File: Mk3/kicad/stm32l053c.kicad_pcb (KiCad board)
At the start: 2 copper layers, 27.2 x 21.8 mm, 29 parts, among them J1 LIGHT+, J2 LIGHT-, P1 SWD, U1 AP2112, U2 STM32L053C8_LQFP48, U3 ADS1015, U4 UFL_SMA, U5 RFM92/95

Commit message: Start of traces
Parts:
- moved C1 4.89 mm to (141.2, 88.9), turned to 90 degrees
- moved C2 2.03 mm to (151.9, 91.2), turned to 270 degrees
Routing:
- net SWO: track 0.00 -> 21.8 mm, vias 0 -> 1
- net SWCLK: track 0.00 -> 20.5 mm, vias 0 -> 1
- net RFM_RST: track 0.00 -> 19.9 mm, vias 0 -> 1
- net SWDIO: track 0.00 -> 19.0 mm, vias 0 -> 1
- net DIO0: track 0.00 -> 14.8 mm, vias 0 -> 1
- net SPI1_MISO: track 0.00 -> 9.81 mm, vias 0 -> 1
- net SPI1_CS: track 0.00 -> 8.83 mm, vias 0 -> 1
- net /AIN2: track 0.00 -> 6.80 mm
- net SPI1_MOSI: track 0.00 -> 5.48 mm, vias 0 -> 1
- net SPI1_SCK: track 0.00 -> 4.49 mm, vias 0 -> 1
- net I2C1_SCL: track 0.00 -> 2.96 mm
- net I2C1_SDA: track 0.00 -> 2.89 mm

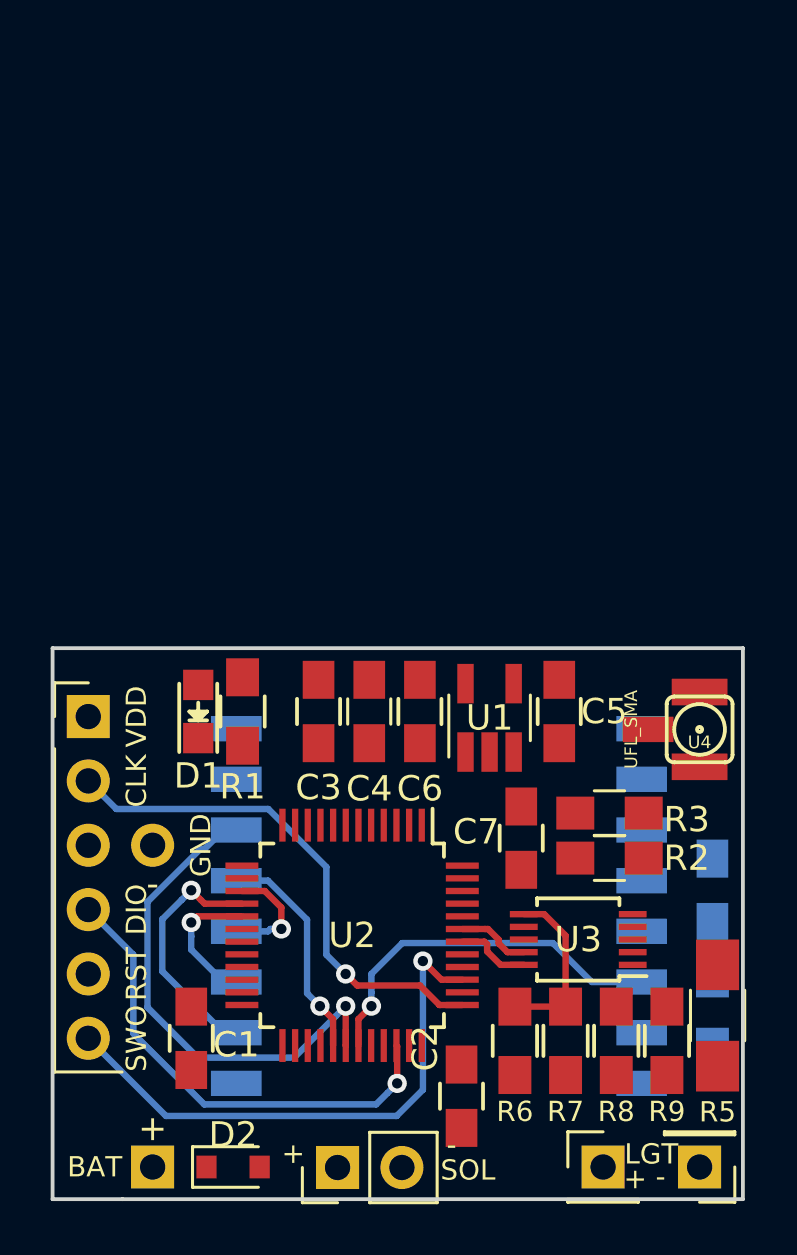
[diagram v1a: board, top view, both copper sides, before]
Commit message: Bigger board
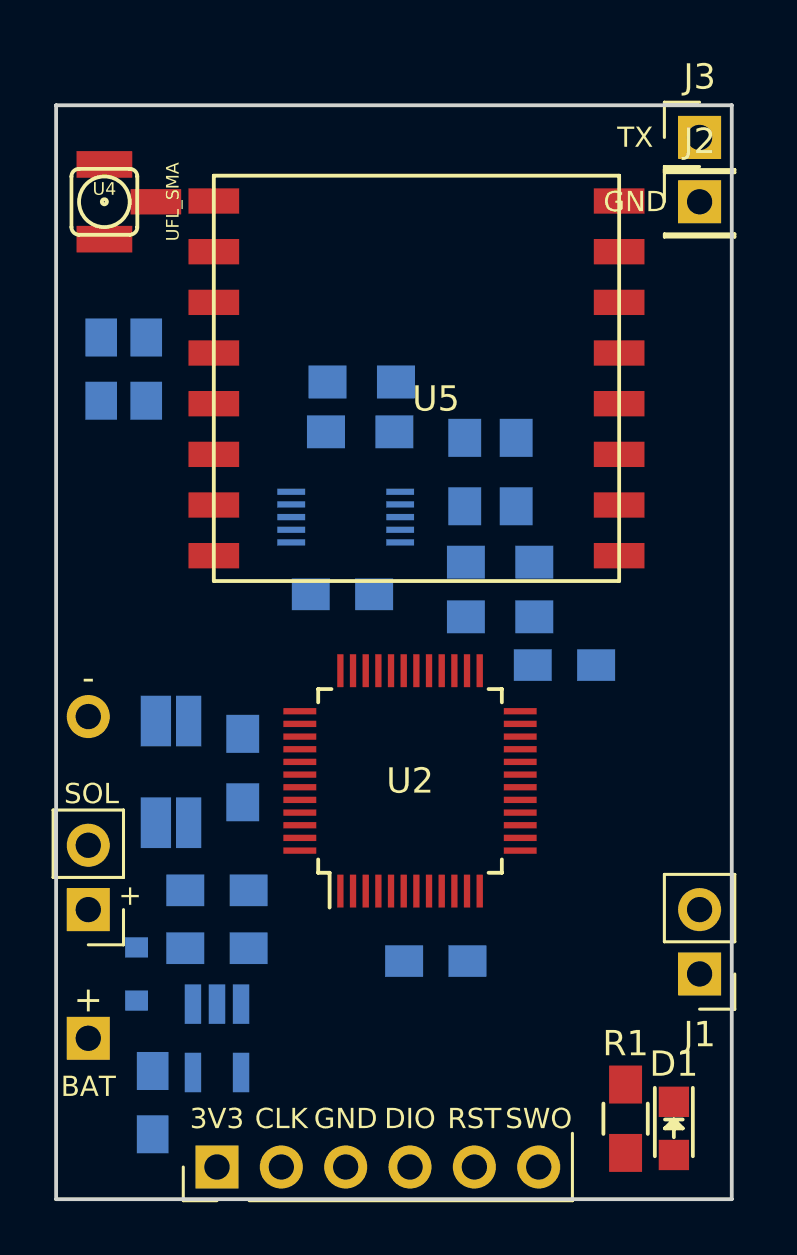
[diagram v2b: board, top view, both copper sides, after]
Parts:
- added J3: TX, Pin_Headers:Pin_Header_Straight_1x01_Pitch2.54mm, F.Cu at (161.3, 53.3)
- C1, C2, C3, C4, C5, C6, C7, D2, R2, R3, R6, R7, R8, R9, U1, U3: moved to B.Cu
- J1: value LIGHT+ -> LGT; footprint Pin_Headers:Pin_Header_Straight_1x01_Pitch2.54mm -> Pin_Headers:Pin_Header_Straight_1x02_Pitch2.54mm
- J2: value LIGHT- -> GND
- R5: value R -> R_Shunt; footprint Resistors_SMD:R_1206_HandSoldering -> theapi:SHUNT_1210_HandSoldering; moved to B.Cu
- U5: moved to F.Cu
- moved J2 38.1 mm to (161.3, 55.9), turned to 0 degrees
- moved U4 31.4 mm to (137.8, 55.9), turned to 90 degrees
- moved C8 30.4 mm to (139.4, 62.5)
- moved R8 27.9 mm to (148.0, 63.0), turned to 180 degrees
- moved R9 26.9 mm to (147.9, 65.0), turned to 180 degrees
- moved U5 25.7 mm to (158.1, 69.8), turned to 180 degrees
- moved D1 25.0 mm to (160.3, 92.5), turned to 270 degrees
- moved R5 23.6 mm to (140.5, 78.4)
- moved R6 22.5 mm to (152.0, 66.5), turned to 270 degrees
- moved R7 22.5 mm to (154.1, 66.5), turned to 90 degrees
- moved R1 22.1 mm to (158.4, 92.1), turned to 270 degrees
- moved R4 20.9 mm to (143.3, 78.2), turned to 90 degrees
- moved C1 20.8 mm to (156.0, 74.2), turned to 0 degrees
- moved U3 19.0 mm to (147.3, 68.3), turned to 0 degrees
- moved C6 18.7 mm to (139.7, 91.4)
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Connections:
- net /PA0 renamed LED
- net Net-(R8-Pad1) renamed /AIN3
- J2 pad 1: LIGHT- -> Earth
- P1 pad 6: SWO -> Net-(P1-Pad6)
- R5 pad 1: /AIN0_1 -> SOL_GND
- R5 pad 2: Earth -> /AIN0
- SC1 pad 2: /AIN0_1 -> SOL_GND
- U2 pad 11: ADC_RDY -> LGT_GND
- U2 pad 12: LIGHT- -> Net-(U2-Pad12)
- U2 pad 15: SPI1_SCK -> Net-(U2-Pad15)
- U2 pad 16: SPI1_MISO -> Net-(U2-Pad16)
- U2 pad 17: SPI1_MOSI -> Net-(U2-Pad17)
- U2 pad 21: Net-(U2-Pad21) -> DIO0
- U2 pad 22: Net-(U2-Pad22) -> RFM_RST
- U2 pad 25: Net-(U2-Pad25) -> SPI2_NSS
- U2 pad 26: Net-(U2-Pad26) -> SPI2_SCK
- U2 pad 27: Net-(U2-Pad27) -> SPI2_MISO
- U2 pad 28: Net-(U2-Pad28) -> SPI2_MOSI
- U2 pad 29: SPI1_CS -> Net-(U2-Pad29)
- U2 pad 30: RFM_RST -> USART1_TX
- U2 pad 31: DIO0 -> Net-(U2-Pad31)
- U2 pad 39: SWO -> Net-(U2-Pad39)
- U2 pad 41: Net-(U2-Pad41) -> ADC_RDY
- U3 pad 4: /AIN0_1 -> /AIN0
- U3 pad 5: Earth -> /AIN1
- U5 pad 2: SPI1_MISO -> SPI2_MISO
- U5 pad 3: SPI1_MOSI -> SPI2_MOSI
- U5 pad 4: SPI1_SCK -> SPI2_SCK
- U5 pad 5: SPI1_CS -> SPI2_NSS
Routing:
- net SWO: track 21.8 -> 0.00 mm, vias 1 -> 0
- net SWCLK: track 20.5 -> 0.00 mm, vias 1 -> 0
- net RFM_RST: track 19.9 -> 0.00 mm, vias 1 -> 0
- net SWDIO: track 19.0 -> 0.00 mm, vias 1 -> 0
- net DIO0: track 14.8 -> 0.00 mm, vias 1 -> 0
- net SPI1_MISO: track 9.81 -> 0.00 mm, vias 1 -> 0
- net SPI1_CS: track 8.83 -> 0.00 mm, vias 1 -> 0
- net /AIN2: track 6.80 -> 0.00 mm
- net SPI1_MOSI: track 5.48 -> 0.00 mm, vias 1 -> 0
- net SPI1_SCK: track 4.49 -> 0.00 mm, vias 1 -> 0
- net I2C1_SCL: track 2.96 -> 0.00 mm
- net I2C1_SDA: track 2.89 -> 0.00 mm
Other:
- board size 27.2 x 21.8 mm -> 26.7 x 43.2 mm
- board text added: "3V3"
- board text added: "TX"
- board text removed: "-"
- board text removed: "LGT"
- board text removed: "VDD"

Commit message: Routing
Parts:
- C2, C3, C4, C7, C8, R4: moved to F.Cu
- D2: footprint Diodes_SMD:D_0805 -> Diodes_SMD:D_1206
- moved R7 7.50 mm to (147.3, 63.2), turned to 180 degrees
- moved R8 5.46 mm to (152.9, 65.3), turned to 0 degrees
- moved R9 5.30 mm to (152.9, 63.2), turned to 0 degrees
- moved R6 4.87 mm to (147.3, 65.3), turned to 0 degrees
- moved C7 4.31 mm to (144.1, 74.4)
- moved C3 1.64 mm to (151.0, 87.5), turned to 270 degrees
- moved C2 1.52 mm to (143.8, 83.1)
- moved R4 0.54 mm to (143.6, 77.9)
- moved R5 0.52 mm to (140.0, 78.5)
- moved C5 0.51 mm to (142.7, 85.3)
- moved D2 0.25 mm to (139.3, 86.4)
- moved R1 0.18 mm to (158.2, 91.9)
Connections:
- U2 pad 21: DIO0 -> Net-(U2-Pad21)
- U2 pad 33: Net-(U2-Pad33) -> DIO0
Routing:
- net +3V3: track 0.00 -> 97.5 mm, vias 0 -> 2
- net USART1_TX: track 0.00 -> 27.3 mm
- net Net-(D2-Pad2): track 0.00 -> 26.0 mm, vias 0 -> 1
- net Net-(J1-Pad1): track 0.00 -> 24.6 mm
- net RFM_RST: track 0.00 -> 23.1 mm
- net SPI2_NSS: track 0.00 -> 20.8 mm
- net SWCLK: track 0.00 -> 20.4 mm, vias 0 -> 1
- net SWDIO: track 0.00 -> 20.3 mm, vias 0 -> 1
- net SPI2_SCK: track 0.00 -> 18.8 mm
- net I2C1_SDA: track 0.00 -> 17.4 mm, vias 0 -> 1
- net NRST: track 0.00 -> 16.0 mm, vias 0 -> 1
- net /AIN0: track 0.00 -> 15.8 mm
- net I2C1_SCL: track 0.00 -> 14.1 mm, vias 0 -> 1
- net LED: track 0.00 -> 13.0 mm
- net SPI2_MOSI: track 0.00 -> 12.2 mm
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
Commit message: Fully routed
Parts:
- C1: moved to F.Cu
- C7: moved to B.Cu
- moved C7 4.58 mm to (147.3, 71.1)
- moved C1 0.36 mm to (155.7, 74.4)
- moved R5 0.25 mm to (139.7, 78.5)
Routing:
- net Earth: track 9.17 -> 216.7 mm, vias 0 -> 11
- net +3V3: track 97.5 -> 117.1 mm, vias 2 -> 1
- net ADC_RDY: track 0.00 -> 14.0 mm, vias 0 -> 1
- net LGT_GND: track 0.00 -> 10.6 mm
- net Net-(D2-Pad2): track 26.0 -> 28.2 mm, vias 1 -> 0
- net SWDIO: track 20.3 -> 22.2 mm
- net SWCLK: track 20.4 -> 22.1 mm
- net USART1_TX: track 27.3 -> 28.5 mm
- net RFM_RST: track 23.1 -> 24.2 mm
- net /AIN0: track 15.8 -> 15.0 mm
- net I2C1_SCL: track 14.1 -> 14.8 mm
- net I2C1_SDA: track 17.4 -> 18.1 mm
- added copper zone on B.Cu, net Earth
- added copper zone on F.Cu, net Earth

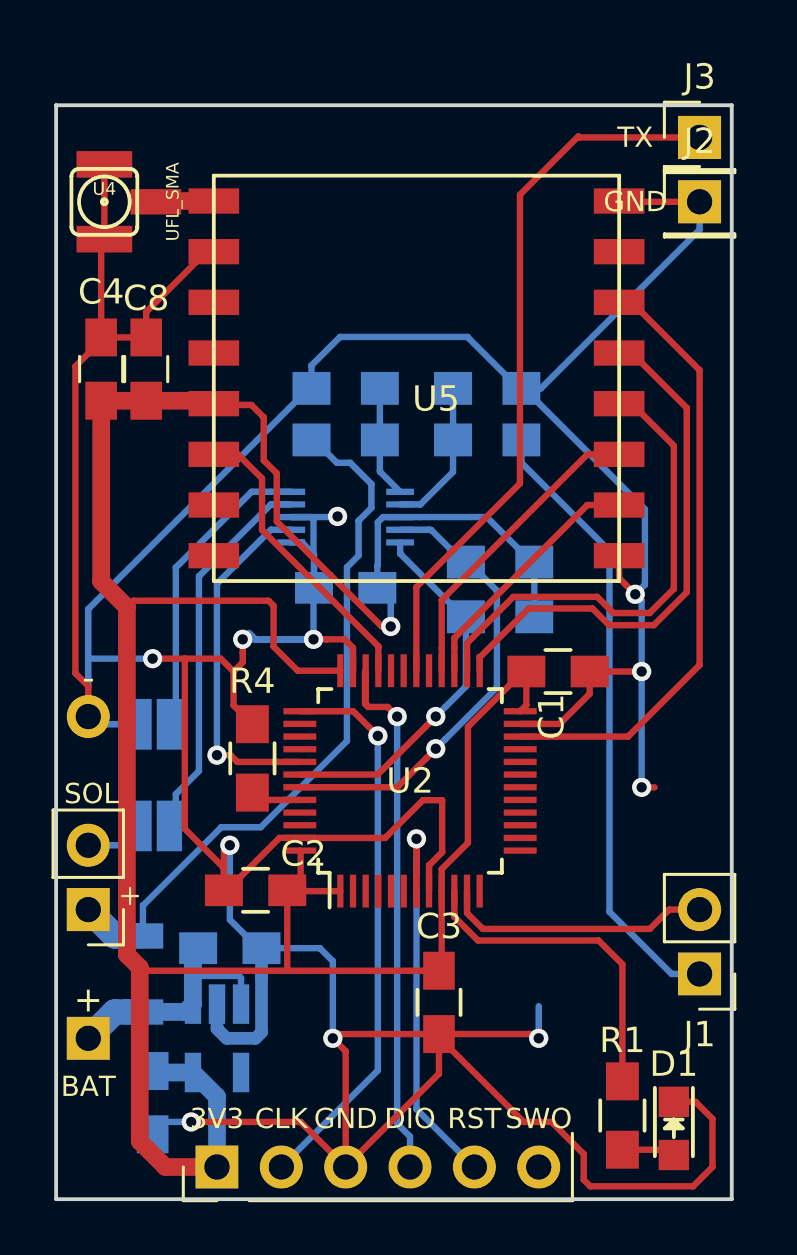
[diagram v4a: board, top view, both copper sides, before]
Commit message: Layout tweaks
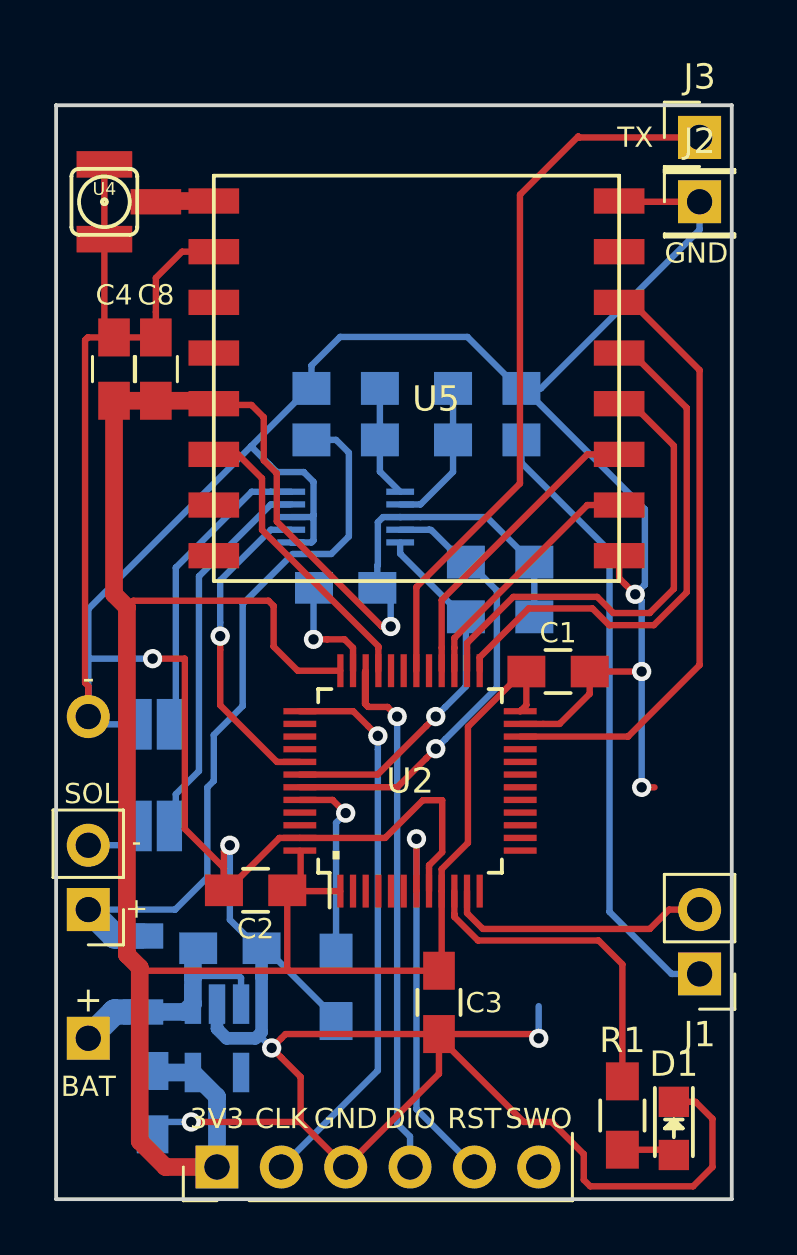
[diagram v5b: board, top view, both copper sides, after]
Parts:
- R4: moved to B.Cu
- moved R4 9.60 mm to (146.9, 86.9), turned to 270 degrees
- moved C4 0.51 mm to (138.2, 62.5)
- moved C8 0.38 mm to (139.8, 62.5)
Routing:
- net Earth: track 216.7 -> 210.1 mm, vias 11 -> 9
- net Net-(R4-Pad1): track 1.99 -> 7.69 mm, vias 0 -> 1
- net ADC_RDY: track 14.0 -> 12.6 mm
- net Net-(D2-Pad2): track 28.2 -> 29.5 mm
- net +3V3: track 117.1 -> 118.0 mm
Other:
- board text added: "-"
- board text added: "."

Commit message: Extra analog inputs
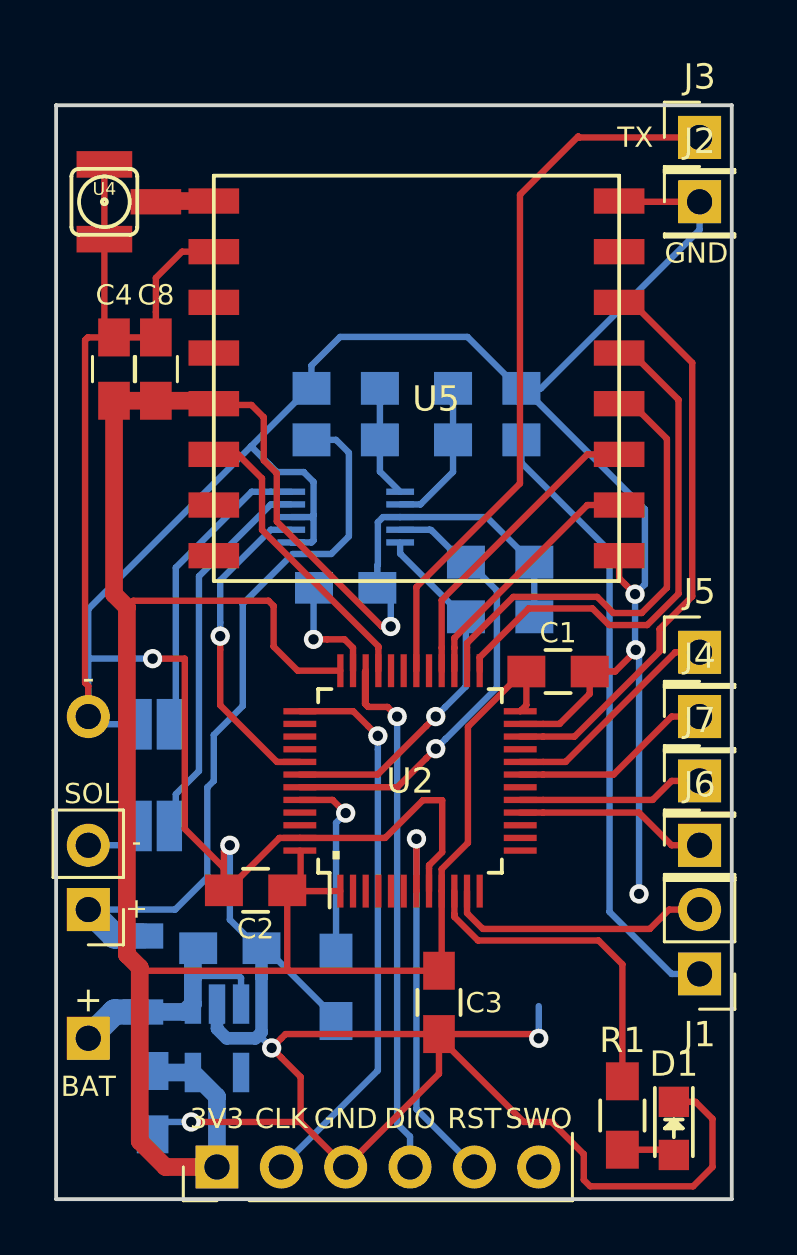
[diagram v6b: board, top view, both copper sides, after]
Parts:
- added J4: A0, Pin_Headers:Pin_Header_Straight_1x01_Pitch2.54mm, F.Cu at (161.3, 76.2)
- added J5: A1, Pin_Headers:Pin_Header_Straight_1x01_Pitch2.54mm, F.Cu at (161.3, 73.7)
- added J6: A3, Pin_Headers:Pin_Header_Straight_1x01_Pitch2.54mm, F.Cu at (161.3, 81.3)
- added J7: A2, Pin_Headers:Pin_Header_Straight_1x01_Pitch2.54mm, F.Cu at (161.3, 78.7)
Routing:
- net Net-(J5-Pad1): track 0.00 -> 8.87 mm
- net Net-(J4-Pad1): track 0.00 -> 8.03 mm
- net Net-(J6-Pad1): track 0.00 -> 7.61 mm
- net Net-(J7-Pad1): track 0.00 -> 7.39 mm
- net Earth: track 210.1 -> 213.9 mm
- net RFM_RST: track 24.2 -> 22.7 mm
